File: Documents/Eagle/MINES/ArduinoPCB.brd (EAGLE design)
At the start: 50.5 x 47 mm, 17 parts, among them IC1 ULN2003AN, IC2 ULN2003AN, X1 B2B-XH-2, X10 B5B-XH-2, X11 B2B-XH-2, X12 B2B-XH-2, X13 B2B-XH-2, X14 B2B-XH-2, X2 B2B-XH-2, X3 B4B-XH-2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

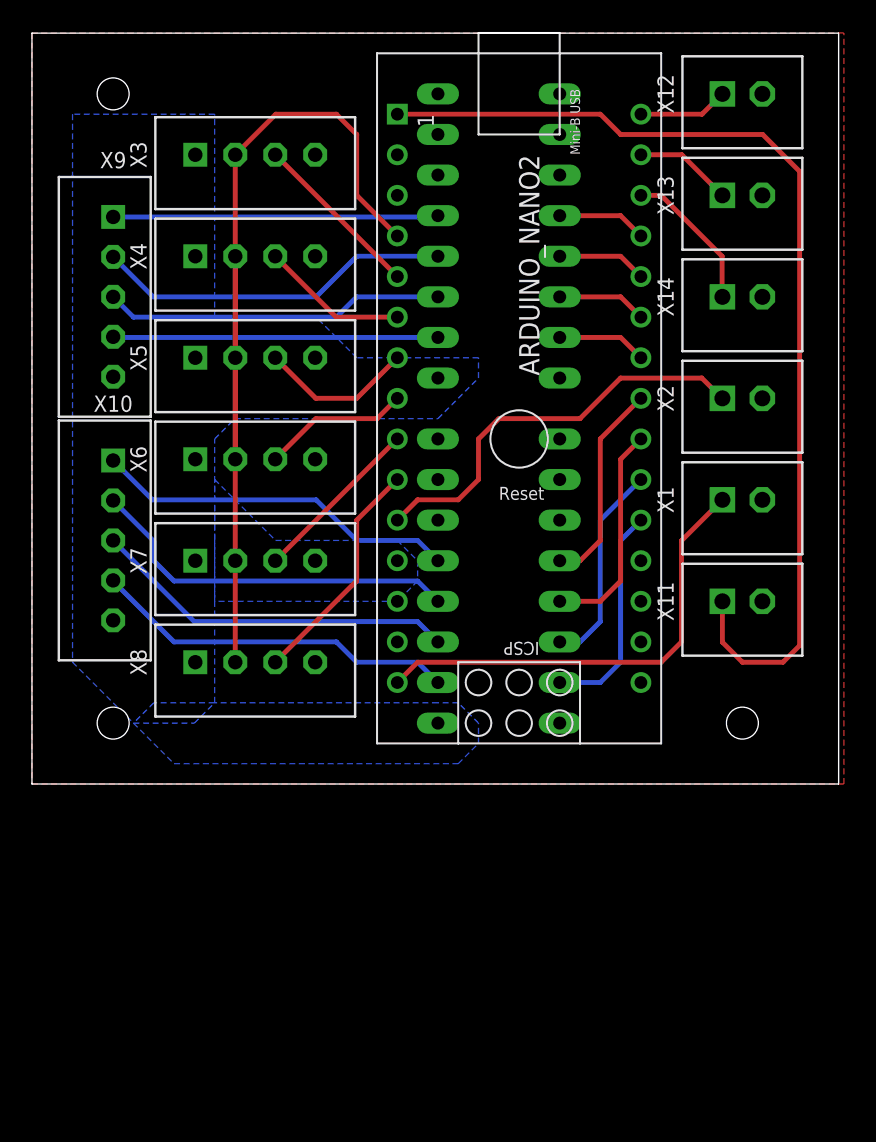
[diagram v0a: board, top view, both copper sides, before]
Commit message: Put 2 arduinos in eagle
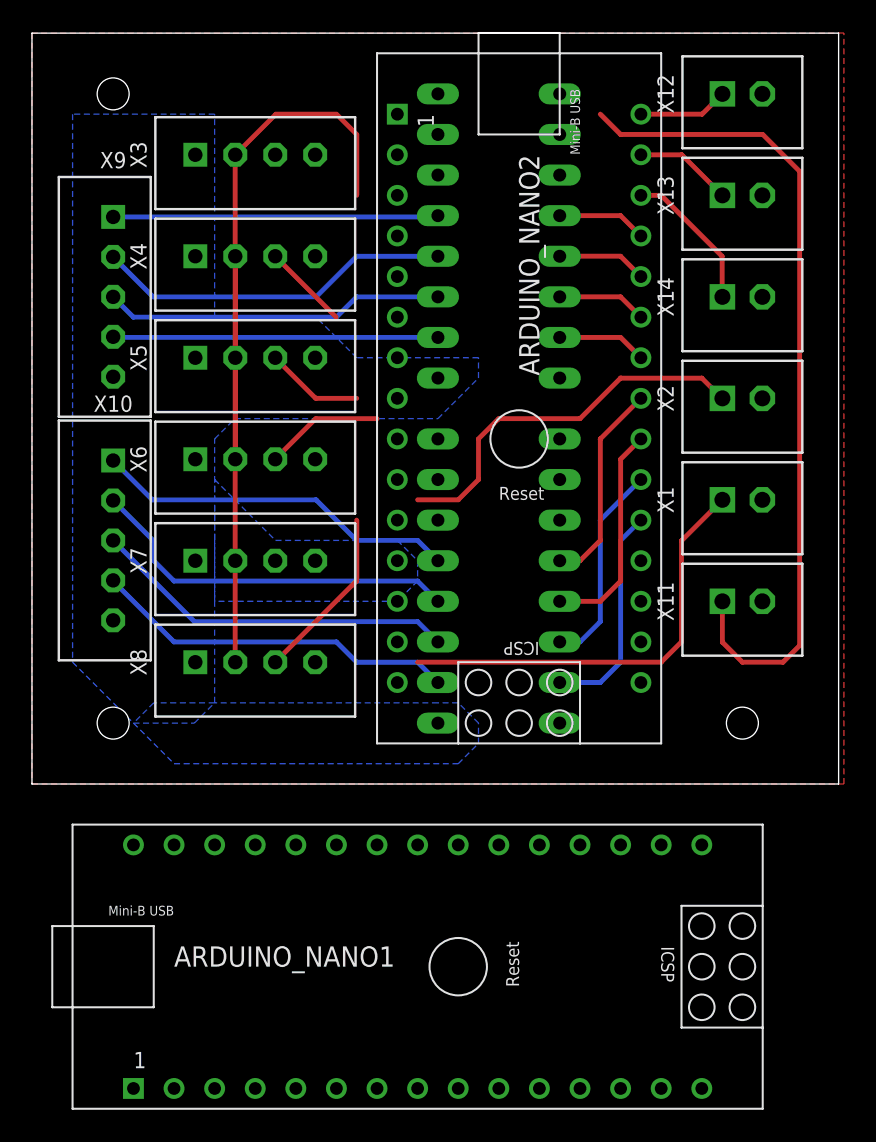
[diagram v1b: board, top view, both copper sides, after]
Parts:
- added ARDUINO_NANO1: (no value), ArduinoNanoV31:ARDUINO_NANO
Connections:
- removed net N$21: ARDUINO_NANO2.14
- net +5V: now also ARDUINO_NANO1.12
- net GND: now also ARDUINO_NANO1.14, ARDUINO_NANO1.19, ARDUINO_NANO2.14
- net N$19: now also ARDUINO_NANO2.4; no longer ARDUINO_NANO2.1
- net N$20: now also ARDUINO_NANO1.15
- net N$22: now also ARDUINO_NANO1.21; no longer ARDUINO_NANO2.11
- net N$24: now also ARDUINO_NANO1.26; no longer ARDUINO_NANO2.9
- net N$25: no longer ARDUINO_NANO2.5
- net N$27: now also ARDUINO_NANO1.29; no longer ARDUINO_NANO2.6
- net N$28: now also ARDUINO_NANO1.28; no longer ARDUINO_NANO2.7
- net N$31: now also ARDUINO_NANO1.27; no longer ARDUINO_NANO2.8
- net N$34: now also ARDUINO_NANO1.30; no longer ARDUINO_NANO2.4
- net N$35: now also ARDUINO_NANO1.25; no longer ARDUINO_NANO2.10
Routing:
- net N$19: track 64.7 -> 52.0 mm
- net N$25: track 10.8 -> 0.02 mm
- net N$24: track 10.8 -> 0.02 mm
- net N$27: track 9.22 -> 5.39 mm
- net N$35: track 14.6 -> 11.0 mm
- net N$28: track 9.74 -> 6.15 mm
- net N$34: track 61.1 -> 57.5 mm
- net N$20: track 28.8 -> 27.0 mm
- net N$31: track 9.22 -> 7.42 mm
- net N$22: track 26.0 -> 24.2 mm
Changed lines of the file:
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@@
 <attribute name="VALUE" x="26.67" y="72.39" size="1.27" layer="21" font="vector" rot="R270"/>
+</element>
+<element name="ARDUINO_NANO1" library="ArduinoNanoV31" package="ARDUINO_NANO" value="" x="25.4" y="21.59" smashed="yes">
+<attribute name="NAME" x="7.62" y="21.59" size="1.27" layer="21" font="vector"/>
+<attribute name="VALUE" x="7.62" y="19.05" size="1.27" layer="21" font="vector"/>
 </element>
 </elements>
@@
 <vertex x="6.35" y="38.1"/>
 </polygon>
+<contactref element="ARDUINO_NANO1" pad="12"/>
 <contactref element="ARDUINO_NANO2" pad="12"/>
-<wire x1="3.81" y1="43.26" x2="8.95" y2="46.99" width="0" layer="19" extent="1-1"/>
+<wire x1="21.59" y1="46.99" x2="24.13" y2="58.42" width="0" layer="19" extent="1-1"/>
+<wire x1="24.13" y1="36.83" x2="21.59" y2="46.99" width="0" layer="19" extent="1-1"/>
+<wire x1="8.95" y1="46.99" x2="21.59" y2="46.99" width="0" layer="19" extent="1-1"/>
+<wire x1="8.95" y1="53.34" x2="8.95" y2="46.99" width="0" layer="19" extent="1-1"/>
+<wire x1="8.95" y1="59.69" x2="8.95" y2="53.34" width="0" layer="19" extent="1-1"/>
+<wire x1="3.81" y1="58.5" x2="8.95" y2="59.69" width="0" layer="19" extent="1-1"/>
+<wire x1="8.95" y1="66.04" x2="8.95" y2="59.69" width="0" layer="19" extent="1-1"/>
+<wire x1="8.95" y1="72.39" x2="8.95" y2="66.04" width="0" layer="19" extent="1-1"/>
+<wire x1="8.95" y1="40.64" x2="8.95" y2="46.99" width="0" layer="19" extent="1-1"/>
+<wire x1="3.81" y1="43.26" x2="8.95" y2="40.64" width="0" layer="19" extent="1-1"/>
+<wire x1="33.02" y1="13.97" x2="24.13" y2="36.83" width="0" layer="19" extent="1-1"/>
 </signal>
 <signal name="N$10">
@@
 </polygon>
 <contactref element="ARDUINO_NANO2" pad="19"/>
+<contactref element="ARDUINO_NANO1" pad="19"/>
+<contactref element="ARDUINO_NANO1" pad="14"/>
+<contactref element="ARDUINO_NANO2" pad="14"/>
+<wire x1="44.43" y1="69.85" x2="44.43" y2="76.2" width="0" layer="19" extent="1-1"/>
+<wire x1="44.43" y1="63.5" x2="44.43" y2="69.85" width="0" layer="19" extent="1-1"/>
+<wire x1="44.43" y1="57.15" x2="44.43" y2="63.5" width="0" layer="19" extent="1-1"/>
+<wire x1="44.43" y1="50.8" x2="44.43" y2="57.15" width="0" layer="19" extent="1-1"/>
+<wire x1="44.43" y1="44.45" x2="44.43" y2="50.8" width="0" layer="19" extent="1-1"/>
+<wire x1="36.83" y1="46.99" x2="44.43" y2="44.45" width="0" layer="19" extent="1-1"/>
+<wire x1="31.75" y1="36.83" x2="36.83" y2="46.99" width="0" layer="19" extent="1-1"/>
+<wire x1="33.02" y1="29.21" x2="31.75" y2="36.83" width="0" layer="19" extent="1-1"/>
+<wire x1="21.59" y1="41.91" x2="31.75" y2="36.83" width="0" layer="19" extent="1-1"/>
+<wire x1="16.45" y1="40.64" x2="21.59" y2="41.91" width="0" layer="19" extent="1-1"/>
+<wire x1="16.45" y1="46.99" x2="16.45" y2="40.64" width="0" layer="19" extent="1-1"/>
+<wire x1="16.45" y1="53.34" x2="16.45" y2="46.99" width="0" layer="19" extent="1-1"/>
+<wire x1="16.45" y1="59.69" x2="16.45" y2="53.34" width="0" layer="19" extent="1-1"/>
+<wire x1="16.45" y1="66.04" x2="16.45" y2="59.69" width="0" layer="19" extent="1-1"/>
 <wire x1="16.45" y1="72.39" x2="16.45" y2="66.04" width="0" layer="19" extent="1-1"/>
+<wire x1="31.75" y1="58.42" x2="36.83" y2="46.99" width="0" layer="19" extent="1-1"/>
+<wire x1="38.1" y1="13.97" x2="33.02" y2="29.21" width="0" layer="19" extent="1-1"/>
 </signal>
 <signal name="N$25">
 <contactref element="X3" pad="3"/>
 <wire x1="13.97" y1="72.39" x2="13.95" y2="72.39" width="0.3048" layer="1"/>
-<contactref element="ARDUINO_NANO2" pad="5"/>
-<wire x1="21.59" y1="64.77" x2="13.97" y2="72.39" width="0.3048" layer="1"/>
 </signal>
 <signal name="N$27">
 <contactref element="X4" pad="3"/>
 <wire x1="17.76" y1="62.23" x2="13.95" y2="66.04" width="0.3048" layer="1"/>
-<contactref element="ARDUINO_NANO2" pad="6"/>
-<wire x1="21.59" y1="62.23" x2="17.76" y2="62.23" width="0.3048" layer="1"/>
+<contactref element="ARDUINO_NANO1" pad="29"/>
+<wire x1="7.62" y1="29.21" x2="17.76" y2="62.23" width="0" layer="19" extent="1-1"/>
 </signal>
 <signal name="N$31">
@@
 <wire x1="16.49" y1="55.88" x2="13.95" y2="53.34" width="0.3048" layer="1"/>
 <wire x1="16.49" y1="55.88" x2="20.32" y2="55.88" width="0.3048" layer="1"/>
-<contactref element="ARDUINO_NANO2" pad="8"/>
-<wire x1="20.32" y1="55.88" x2="21.59" y2="57.15" width="0.3048" layer="1"/>
+<contactref element="ARDUINO_NANO1" pad="27"/>
+<wire x1="12.7" y1="29.21" x2="13.95" y2="53.34" width="0" layer="19" extent="1-1"/>
 </signal>
 <signal name="N$34">
@@
 <wire x1="11.45" y1="40.66" x2="11.44" y2="40.65" width="0.3048" layer="1"/>
 <wire x1="11.45" y1="59.69" x2="11.45" y2="66.04" width="0.3048" layer="1"/>
-<contactref element="ARDUINO_NANO2" pad="4"/>
-<wire x1="21.59" y1="67.31" x2="19.05" y2="69.85" width="0.3048" layer="1"/>
+<contactref element="ARDUINO_NANO1" pad="30"/>
+<wire x1="5.08" y1="29.21" x2="11.45" y2="40.64" width="0" layer="19" extent="1-1"/>
 </signal>
 <signal name="N$35">
@@
 <wire x1="19.03" y1="45.72" x2="19.05" y2="45.72" width="0.3048" layer="1"/>
 <wire x1="19.05" y1="45.72" x2="19.05" y2="49.53" width="0.3048" layer="1"/>
-<contactref element="ARDUINO_NANO2" pad="10"/>
-<wire x1="19.05" y1="49.53" x2="21.59" y2="52.07" width="0.3048" layer="1"/>
+<contactref element="ARDUINO_NANO1" pad="25"/>
+<wire x1="17.78" y1="29.21" x2="13.95" y2="40.64" width="0" layer="19" extent="1-1"/>
 </signal>
 <signal name="N$20">
@@
 <wire x1="22.86" y1="40.64" x2="38.1" y2="40.64" width="0.3048" layer="1"/>
 <wire x1="39.37" y1="41.91" x2="39.37" y2="48.24" width="0.3048" layer="1"/>
+<contactref element="ARDUINO_NANO1" pad="15"/>
 <contactref element="ARDUINO_NANO2" pad="15"/>
-<wire x1="21.59" y1="39.37" x2="22.86" y2="40.64" width="0.3048" layer="1"/>
+<wire x1="21.59" y1="39.37" x2="22.86" y2="40.64" width="0" layer="19" extent="1-1"/>
+<wire x1="40.64" y1="13.97" x2="21.59" y2="39.37" width="0" layer="19" extent="1-1"/>
 </signal>
 <signal name="N$22">
@@
 <wire x1="25.4" y1="50.8" x2="22.86" y2="50.8" width="0.3048" layer="1"/>
 <wire x1="33.02" y1="55.88" x2="27.94" y2="55.88" width="0.3048" layer="1"/>
-<contactref element="ARDUINO_NANO2" pad="11"/>
-<wire x1="22.86" y1="50.8" x2="21.59" y2="49.53" width="0.3048" layer="1"/>
+<contactref element="ARDUINO_NANO1" pad="21"/>
+<wire x1="27.94" y1="29.21" x2="22.86" y2="50.8" width="0" layer="19" extent="1-1"/>
 </signal>
 <signal name="N$1">
@@
 <wire x1="43.18" y1="40.64" x2="41.93" y2="41.89" width="0.3048" layer="1"/>
 <wire x1="41.93" y1="41.89" x2="41.93" y2="44.45" width="0.3048" layer="1"/>
-<contactref element="ARDUINO_NANO2" pad="1"/>
-<wire x1="34.29" y1="74.93" x2="21.59" y2="74.93" width="0.3048" layer="1"/>
+<contactref element="ARDUINO_NANO2" pad="4"/>
+<wire x1="34.29" y1="74.93" x2="21.59" y2="67.31" width="0" layer="19" extent="1-1"/>
 </signal>
 <signal name="N$24">
 <contactref element="X7" pad="3"/>
 <wire x1="13.97" y1="46.99" x2="13.95" y2="46.99" width="0.3048" layer="1"/>
-<contactref element="ARDUINO_NANO2" pad="9"/>
-<wire x1="21.59" y1="54.61" x2="13.97" y2="46.99" width="0.3048" layer="1"/>
+<contactref element="ARDUINO_NANO1" pad="26"/>
+<wire x1="15.24" y1="29.21" x2="13.95" y2="46.99" width="0" layer="19" extent="1-1"/>
 </signal>
 <signal name="N$28">
@@
 <wire x1="16.49" y1="57.15" x2="19.05" y2="57.15" width="0.3048" layer="1"/>
 <wire x1="16.49" y1="57.15" x2="13.95" y2="59.69" width="0.3048" layer="1"/>
-<contactref element="ARDUINO_NANO2" pad="7"/>
-<wire x1="19.05" y1="57.15" x2="21.59" y2="59.69" width="0.3048" layer="1"/>
-</signal>
-<signal name="N$21">
-<contactref element="ARDUINO_NANO2" pad="14"/>
+<contactref element="ARDUINO_NANO1" pad="28"/>
+<wire x1="10.16" y1="29.21" x2="19.05" y2="57.15" width="0" layer="19" extent="1-1"/>
 </signal>
 </signals>
